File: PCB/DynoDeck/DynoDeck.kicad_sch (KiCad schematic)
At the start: 76 parts, among them J1 USB_C_Receptacle_USB2.0_16P, J2 PGRM, J3 CardKBConn, J4 E-paper, J5 HC-IPEX0125-01 (u.FL), J6 BWSMA-KWE-Z001 (SMA), J7 CardKBRef, SW1 QON, SW2 POWER, SW3 RESET, SW4 IO1, U1 BQ25895RTW, U2 USBLC6-2SC6, U3 SX1262IMLTRT, U4 TUSB320, U5 MD7218E33PC1, U6 E73-2G4M08S1C, U7 PE42422MLAA-Z, U8 PE42422MLAA-Z, Y1 OW7EL89CENUXK7YLC-32M, Y3 3N00032G33YC

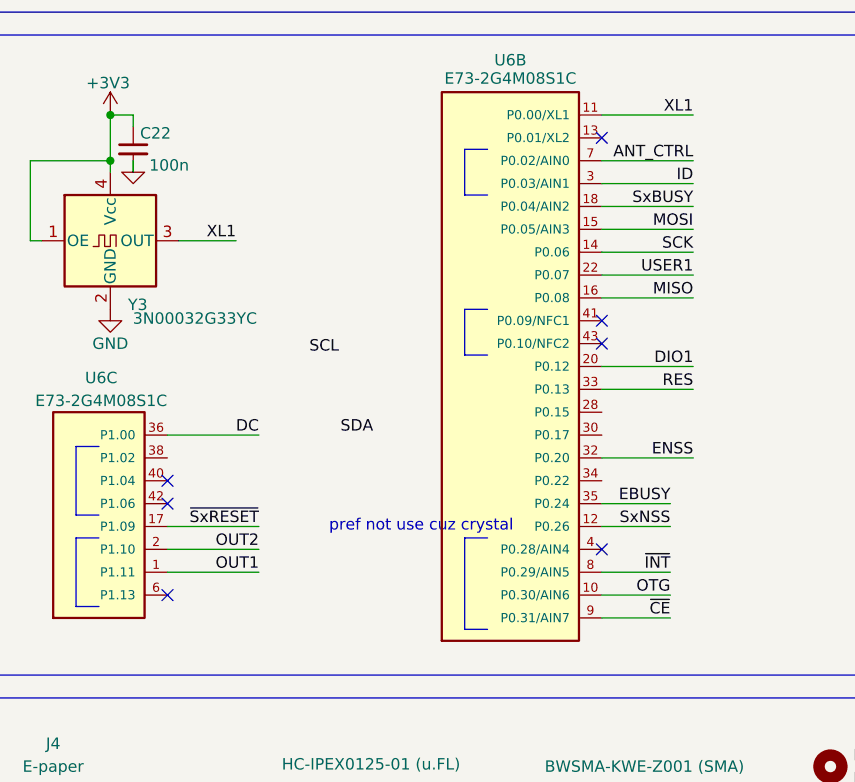
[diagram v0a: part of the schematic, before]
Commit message: TUSB320 wiring to nRF
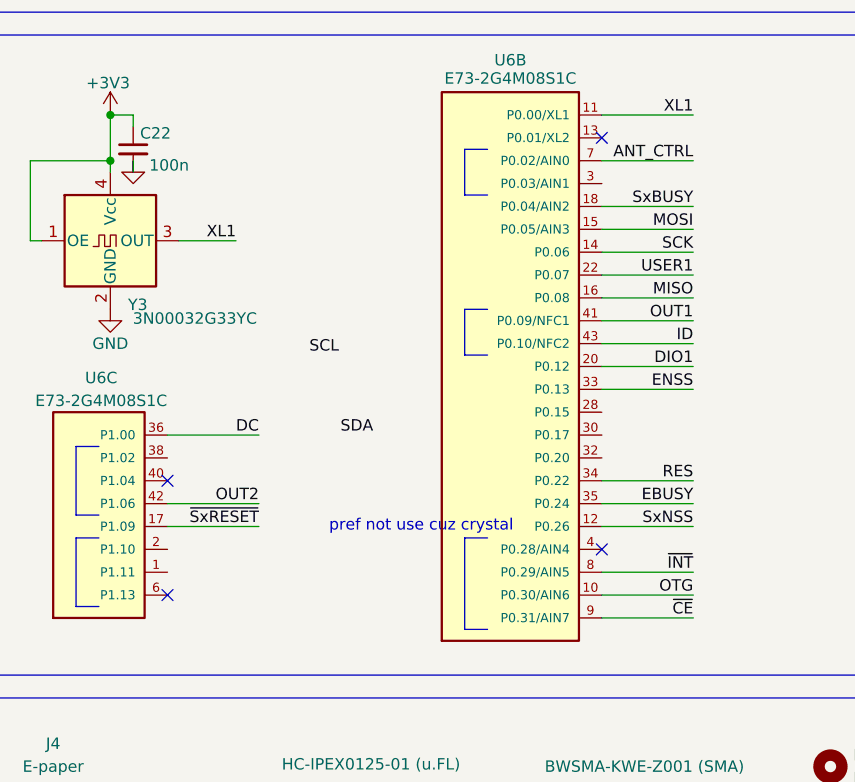
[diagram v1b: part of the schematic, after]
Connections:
- net ENSS: now also U6.33 (P0.13); no longer U6.32 (P0.20)
- net ID: now also U6.43 (P0.10/NFC2); no longer U6.3 (P0.03/AIN1)
- net OUT1: now also U6.41 (P0.09/NFC1); no longer U6.1 (P1.11)
- net OUT2: now also U6.42 (P1.06); no longer U6.2 (P1.10)
- net RES: now also U6.34 (P0.22); no longer U6.33 (P0.13)
- no-connect marks 20 -> 17
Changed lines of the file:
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@@
 	)
 	(no_connect
-		(at 302.26 100.33)
-	)
-	(no_connect
 		(at 194.31 172.72)
 	)
 	(no_connect
-		(at 254 118.11)
-	)
-	(no_connect
-		(at 302.26 97.79)
-	)
-	(no_connect
 		(at 254 128.27)
 	)
@@
 	(wire
 		(pts
-			(xy 242.57 54.61) (xy 254 54.61)
+			(xy 254 118.11) (xy 264.16 118.11)
 		)
 		(stroke
@@
 	(wire
 		(pts
-			(xy 57.15 143.51) (xy 64.77 143.51)
+			(xy 242.57 54.61) (xy 254 54.61)
 		)
 		(stroke
@@
 	(wire
 		(pts
-			(xy 129.54 105.41) (xy 134.62 105.41)
+			(xy 57.15 143.51) (xy 64.77 143.51)
 		)
 		(stroke
@@
 	(wire
 		(pts
-			(xy 302.26 120.65) (xy 309.88 120.65)
+			(xy 129.54 105.41) (xy 134.62 105.41)
 		)
 		(stroke
@@
 	(wire
 		(pts
-			(xy 302.26 113.03) (xy 312.42 113.03)
-		)
-		(stroke
-			(width 0)
-			(type default)
-		)
-	)
-	(wire
-		(pts
 			(xy 34.29 129.54) (xy 41.91 129.54)
 		)
@@
 		)
 	)
-	(wire
-		(pts
-			(xy 302.26 105.41) (xy 312.42 105.41)
-		)
-		(stroke
-			(width 0)
-			(type default)
-		)
-	)
 	(polyline
 		(pts
@@
 	(wire
 		(pts
+			(xy 302.26 115.57) (xy 312.42 115.57)
+		)
+		(stroke
+			(width 0)
+			(type default)
+		)
+	)
+	(wire
+		(pts
 			(xy 302.26 95.25) (xy 312.42 95.25)
 		)
@@
 	(wire
 		(pts
+			(xy 302.26 130.81) (xy 312.42 130.81)
+		)
+		(stroke
+			(width 0)
+			(type default)
+		)
+	)
+	(wire
+		(pts
 			(xy 93.98 83.82) (xy 96.52 83.82)
 		)
@@
 	(wire
 		(pts
-			(xy 302.26 102.87) (xy 312.42 102.87)
+			(xy 302.26 105.41) (xy 312.42 105.41)
 		)
 		(stroke
@@
 		)
 	)
-	(polyline
+	(wire
 		(pts
-			(xy 233.68 170.18) (xy 233.68 200.66)
+			(xy 302.26 102.87) (xy 312.42 102.87)
 		)
 		(stroke
@@
 		)
 	)
-	(wire
+	(polyline
 		(pts
-			(xy 240.03 46.99) (xy 243.84 46.99)
+			(xy 233.68 170.18) (xy 233.68 200.66)
 		)
 		(stroke
@@
 	(wire
 		(pts
-			(xy 182.88 120.65) (xy 187.96 120.65)
+			(xy 240.03 46.99) (xy 243.84 46.99)
 		)
 		(stroke
@@
 	(wire
 		(pts
-			(xy 302.26 125.73) (xy 309.88 125.73)
+			(xy 182.88 120.65) (xy 187.96 120.65)
 		)
 		(stroke
@@
 	(wire
 		(pts
-			(xy 50.8 120.65) (xy 50.8 129.54)
+			(xy 302.26 120.65) (xy 312.42 120.65)
 		)
 		(stroke
@@
 	(wire
 		(pts
-			(xy 302.26 130.81) (xy 309.88 130.81)
+			(xy 50.8 120.65) (xy 50.8 129.54)
 		)
 		(stroke
@@
 	(wire
 		(pts
+			(xy 302.26 97.79) (xy 312.42 97.79)
+		)
+		(stroke
+			(width 0)
+			(type default)
+		)
+	)
+	(wire
+		(pts
 			(xy 58.42 24.13) (xy 58.42 25.4)
 		)
@@
 	(wire
 		(pts
+			(xy 302.26 125.73) (xy 312.42 125.73)
+		)
+		(stroke
+			(width 0)
+			(type default)
+		)
+	)
+	(wire
+		(pts
 			(xy 129.54 92.71) (xy 129.54 96.52)
 		)
@@
 	(wire
 		(pts
-			(xy 302.26 118.11) (xy 309.88 118.11)
-		)
-		(stroke
-			(width 0)
-			(type default)
-		)
-	)
-	(wire
-		(pts
 			(xy 157.48 152.4) (xy 157.48 153.67)
 		)
@@
 	(wire
 		(pts
-			(xy 302.26 128.27) (xy 309.88 128.27)
-		)
-		(stroke
-			(width 0)
-			(type default)
-		)
-	)
-	(wire
-		(pts
 			(xy 226.06 156.21) (xy 234.95 156.21)
 		)
@@
 	(wire
 		(pts
+			(xy 302.26 118.11) (xy 312.42 118.11)
+		)
+		(stroke
+			(width 0)
+			(type default)
+		)
+	)
+	(wire
+		(pts
 			(xy 110.49 27.94) (xy 110.49 24.13)
 		)
@@
 	(wire
 		(pts
-			(xy 130.81 24.13) (xy 127 24.13)
+			(xy 302.26 128.27) (xy 312.42 128.27)
 		)
 		(stroke
@@
 	(wire
 		(pts
-			(xy 302.26 82.55) (xy 312.42 82.55)
+			(xy 130.81 24.13) (xy 127 24.13)
 		)
 		(stroke
@@
 	(wire
 		(pts
-			(xy 254 125.73) (xy 264.16 125.73)
-		)
-		(stroke
-			(width 0)
-			(type default)
-		)
-	)
-	(wire
-		(pts
 			(xy 302.26 90.17) (xy 312.42 90.17)
 		)
@@
 	(wire
 		(pts
+			(xy 302.26 100.33) (xy 312.42 100.33)
+		)
+		(stroke
+			(width 0)
+			(type default)
+		)
+	)
+	(wire
+		(pts
 			(xy 127 172.72) (xy 127 171.45)
 		)
@@
 	(wire
 		(pts
-			(xy 254 123.19) (xy 264.16 123.19)
-		)
-		(stroke
-			(width 0)
-			(type default)
-		)
-	)
-	(wire
-		(pts
 			(xy 90.17 129.54) (xy 93.98 129.54)
 		)
@@
 	)
 	(label "OUT2"
-		(at 264.16 123.19 180)
+		(at 264.16 118.11 180)
 		(effects
 			(font
@@
 	)
 	(label "ID"
-		(at 312.42 82.55 180)
+		(at 312.42 100.33 180)
 		(effects
 			(font
@@
 	)
 	(label "OTG"
-		(at 309.88 128.27 180)
+		(at 312.42 128.27 180)
 		(effects
 			(font
@@
 	)
 	(label "~{CE}"
-		(at 309.88 130.81 180)
+		(at 312.42 130.81 180)
 		(effects
 			(font
@@
 	)
 	(label "RES"
-		(at 312.42 105.41 180)
+		(at 312.42 115.57 180)
 		(effects
 			(font
@@
 	)
 	(label "~{INT}"
-		(at 309.88 125.73 180)
+		(at 312.42 125.73 180)
 		(effects
 			(font
@@
 	)
 	(label "SxNSS"
-		(at 309.88 120.65 180)
+		(at 312.42 120.65 180)
 		(effects
 			(font
@@
 	)
 	(label "OUT1"
-		(at 264.16 125.73 180)
+		(at 312.42 97.79 180)
 		(effects
 			(font
@@
 	)
 	(label "ENSS"
-		(at 312.42 113.03 180)
+		(at 312.42 105.41 180)
 		(effects
 			(font
@@
 	)
 	(label "EBUSY"
-		(at 309.88 118.11 180)
+		(at 312.42 118.11 180)
 		(effects
 			(font

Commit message: nRF wiring finish I think
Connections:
- net OTG: now also U6.9 (P0.31/AIN7); no longer U6.10 (P0.30/AIN6)
- net SCL: now also U6.30 (P0.17)
- net SDA: now also U6.28 (P0.15)
- net ~{CE}: now also U6.10 (P0.30/AIN6); no longer U6.9 (P0.31/AIN7)
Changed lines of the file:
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@@
 	(wire
 		(pts
-			(xy 302.26 130.81) (xy 312.42 130.81)
-		)
-		(stroke
-			(width 0)
-			(type default)
-		)
-	)
-	(wire
-		(pts
 			(xy 93.98 83.82) (xy 96.52 83.82)
 		)
@@
 		)
 	)
+	(wire
+		(pts
+			(xy 302.26 130.81) (xy 312.42 130.81)
+		)
+		(stroke
+			(width 0)
+			(type default)
+		)
+	)
 	(polyline
 		(pts
@@
 	(wire
 		(pts
+			(xy 302.26 110.49) (xy 312.42 110.49)
+		)
+		(stroke
+			(width 0)
+			(type default)
+		)
+	)
+	(wire
+		(pts
 			(xy 127 22.86) (xy 127 24.13)
 		)
@@
 	(wire
 		(pts
+			(xy 302.26 107.95) (xy 312.42 107.95)
+		)
+		(stroke
+			(width 0)
+			(type default)
+		)
+	)
+	(wire
+		(pts
 			(xy 54.61 109.22) (xy 66.04 109.22)
 		)
@@
 	(wire
 		(pts
-			(xy 302.26 128.27) (xy 312.42 128.27)
+			(xy 130.81 24.13) (xy 127 24.13)
 		)
 		(stroke
@@
 	(wire
 		(pts
-			(xy 130.81 24.13) (xy 127 24.13)
+			(xy 302.26 128.27) (xy 312.42 128.27)
 		)
 		(stroke
@@
 	)
 	(label "OTG"
-		(at 312.42 128.27 180)
+		(at 312.42 130.81 180)
 		(effects
 			(font
@@
 	)
 	(label "~{CE}"
-		(at 312.42 130.81 180)
+		(at 312.42 128.27 180)
 		(effects
 			(font
@@
 	)
 	(label "SCL"
-		(at 273.05 101.6 180)
+		(at 312.42 110.49 180)
 		(effects
 			(font
@@
 	)
 	(label "SDA"
-		(at 276.86 110.49 180)
+		(at 312.42 107.95 180)
 		(effects
 			(font

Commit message: pcb done?
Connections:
- no-connect marks 17 -> 22
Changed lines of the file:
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@@
+	)
+	(no_connect
+		(at 302.26 113.03)
 	)
 	(no_connect
@@
 	)
 	(no_connect
+		(at 254 113.03)
+	)
+	(no_connect
+		(at 302.26 82.55)
+	)
+	(no_connect
 		(at 194.31 172.72)
+	)
+	(no_connect
+		(at 254 123.19)
 	)
 	(no_connect
@@
 	)
 	(no_connect
+		(at 254 125.73)
+	)
+	(no_connect

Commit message: Update mounting hole + DRC stuff
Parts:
- added H3: MountingHole, MountingHole:MountingHole_2.7mm_M2.5, symbol Mechanical:MountingHole
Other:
- moved on the sheet: H1, H2
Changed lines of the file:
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@@
 	(symbol
 		(lib_id "Mechanical:MountingHole")
-		(at 327.66 160.02 0)
+		(at 327.66 146.05 0)
 		(unit 1)
 		(body_style 1)
@@
 		(fields_autoplaced yes)
 		(property "Reference" "H1"
-			(at 330.2 158.7499 0)
+			(at 330.2 144.7799 0)
 			(show_name no)
 			(do_not_autoplace no)
@@
 		)
 		(property "Value" "MountBTML"
-			(at 330.2 161.2899 0)
+			(at 330.2 147.3199 0)
 			(show_name no)
 			(do_not_autoplace no)
@@
 		)
 		(property "Footprint" "MountingHole:MountingHole_2.7mm_M2.5"
-			(at 327.66 160.02 0)
+			(at 327.66 146.05 0)
 			(hide yes)
 			(show_name no)
@@
 		)
 		(property "Datasheet" ""
-			(at 327.66 160.02 0)
+			(at 327.66 146.05 0)
 			(hide yes)
 			(show_name no)
@@
 		)
 		(property "Description" "Mounting Hole without connection"
-			(at 327.66 160.02 0)
+			(at 327.66 146.05 0)
 			(hide yes)
 			(show_name no)
@@
 	(symbol
 		(lib_id "Mechanical:MountingHole")
-		(at 327.66 147.32 0)
+		(at 327.66 152.4 0)
 		(unit 1)
 		(body_style 1)
@@
 		(fields_autoplaced yes)
 		(property "Reference" "H2"
-			(at 330.2 146.0499 0)
+			(at 330.2 151.1299 0)
 			(show_name no)
 			(do_not_autoplace no)
@@
 		)
 		(property "Value" "MountBTMR"
-			(at 330.2 148.5899 0)
+			(at 330.2 153.6699 0)
 			(show_name no)
 			(do_not_autoplace no)
@@
 		)
 		(property "Footprint" "MountingHole:MountingHole_2.7mm_M2.5"
-			(at 327.66 147.32 0)
+			(at 327.66 152.4 0)
 			(hide yes)
 			(show_name no)
@@
 		)
 		(property "Datasheet" ""
-			(at 327.66 147.32 0)
+			(at 327.66 152.4 0)
 			(hide yes)
 			(show_name no)
@@
 		)
 		(property "Description" "Mounting Hole without connection"
-			(at 327.66 147.32 0)
+			(at 327.66 152.4 0)
 			(hide yes)
 			(show_name no)
@@
 				)
 			)
+		)
+	)
+	(symbol
+		(lib_id "Mechanical:MountingHole")
+		(at 327.66 158.75 0)
+		(unit 1)
+		(body_style 1)
+		(exclude_from_sim no)
+		(in_bom no)
+		(on_board yes)
+		(in_pos_files yes)
+		(dnp no)
+		(fields_autoplaced yes)
+		(property "Reference" "H3"
+			(at 330.2 157.4799 0)
+			(show_name no)
+			(do_not_autoplace no)
+			(effects
+				(font
+					(size 1.27 1.27)
+				)
+				(justify left)
+			)
+		)
+		(property "Value" "MountingHole"
+			(at 330.2 160.0199 0)
+			(show_name no)
+			(do_not_autoplace no)
+			(effects
+				(font
+					(size 1.27 1.27)
+				)
+				(justify left)
+			)
+		)
+		(property "Footprint" "MountingHole:MountingHole_2.7mm_M2.5"
+			(at 327.66 158.75 0)
+			(hide yes)
+			(show_name no)
+			(do_not_autoplace no)
+			(effects
+				(font
+					(size 1.27 1.27)
+				)
+			)
+		)
+		(property "Datasheet" ""
+			(at 327.66 158.75 0)
+			(hide yes)
+			(show_name no)
+			(do_not_autoplace no)
+			(effects
+				(font
+					(size 1.27 1.27)
+				)
+			)
+		)
+		(property "Description" "Mounting Hole without connection"
+			(at 327.66 158.75 0)
+			(hide yes)
+			(show_name no)
+			(do_not_autoplace no)
+			(effects
+				(font
+					(size 1.27 1.27)
+				)
+			)
+		)
+		(instances
+			(project "DynoDeck"
+				(path "/d751e66f-06ea-4bc9-898a-20a2be86c932"
+					(reference "H3")
+					(unit 1)
+				)
+			)
